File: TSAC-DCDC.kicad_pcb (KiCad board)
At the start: 2 copper layers, 30 parts, among them IC1 PS2811-1-A, Q2 IPB95R450PFD7ATMA1, U1 UCC28C44DR, U3 TL432DBZ

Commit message: Initial PCB layout
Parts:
- moved C2 142.6 mm to (203.1, 70.8)
- moved Rfbt1 141.0 mm to (207.0, 72.3)
- moved Rfbb1 140.7 mm to (207.0, 68.1)
- moved Ropt1 133.2 mm to (198.1, 70.3), turned to -90 degrees
- moved Rtl1 127.1 mm to (198.0, 64.1), turned to 90 degrees
- moved U3 108.2 mm to (198.9, 76.6)
- moved IC1 73.3 mm to (148.5, 77.5)
- moved Rfb4 65.9 mm to (98.3, 96.0)
- moved Rfb3 57.9 mm to (93.9, 86.8)
- moved Rs1 55.7 mm to (98.2, 84.2)
- moved Rs2 55.7 mm to (98.2, 86.8)
- moved Cdd1 54.9 mm to (65.0, 94.2)
- moved Cfb3 48.3 mm to (94.3, 80.5)
- moved Q2 39.3 mm to (119.0, 78.0)
- moved Rdd1 36.7 mm to (80.0, 84.2)
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
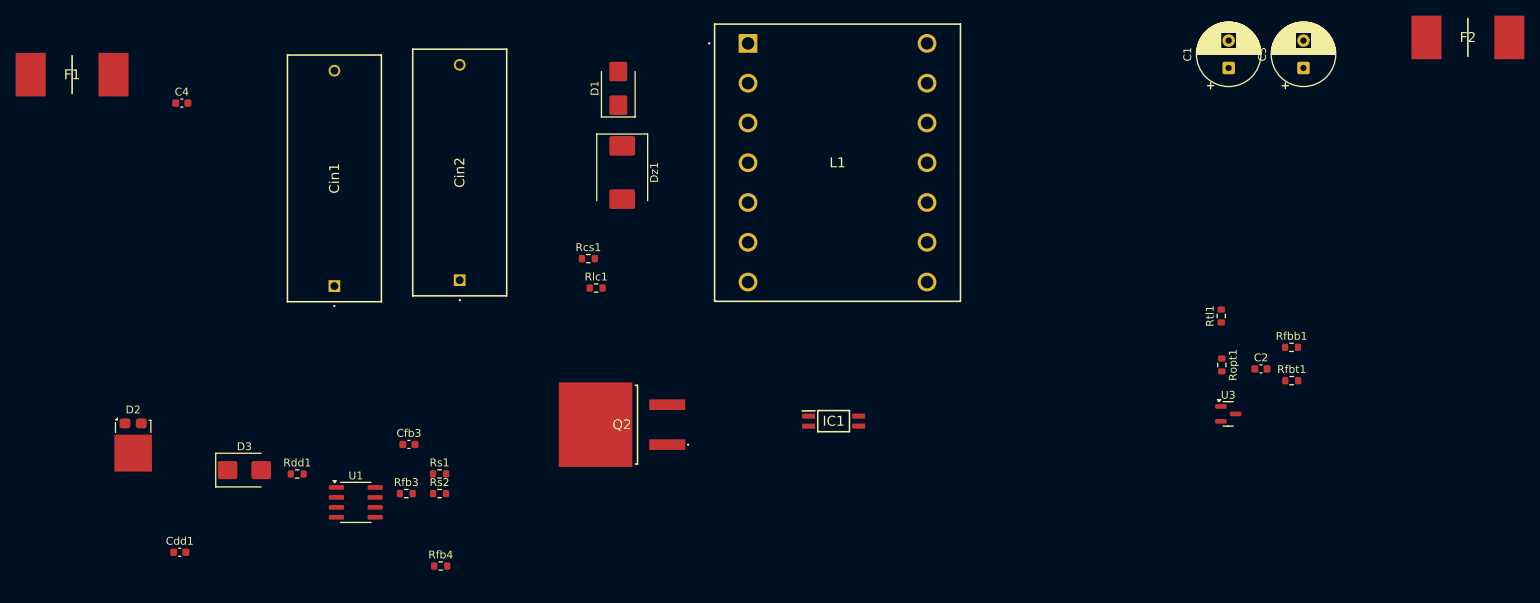
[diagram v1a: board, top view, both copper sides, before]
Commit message: Revert "Initial PCB layout"
This reverts commit eb11546efb0268227655b0bea42a16ad7d7093c5.
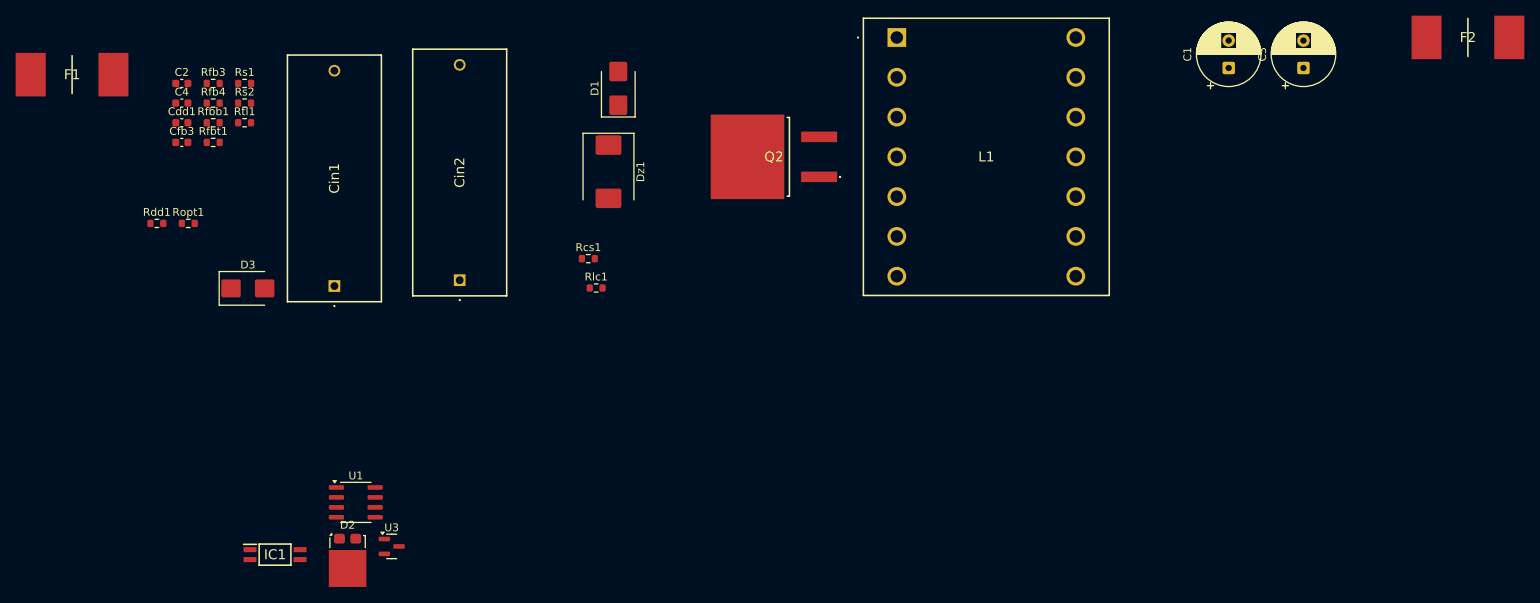
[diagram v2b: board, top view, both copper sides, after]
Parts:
- moved C2 142.6 mm to (65.3, 34.4)
- moved Rfbt1 141.0 mm to (69.3, 41.9)
- moved Rfbb1 140.7 mm to (69.3, 39.4)
- moved Ropt1 133.2 mm to (66.1, 52.2), turned to 0 degrees
- moved Rtl1 127.1 mm to (73.3, 39.4), turned to 0 degrees
- moved U3 108.2 mm to (92.1, 93.5)
- moved IC1 73.3 mm to (77.2, 94.5)
- moved Rfb4 65.9 mm to (69.3, 36.9)
- moved Rfb3 57.9 mm to (69.3, 34.4)
- moved Rs1 55.7 mm to (73.3, 34.4)
- moved Rs2 55.7 mm to (73.3, 36.9)
- moved Cdd1 54.9 mm to (65.3, 39.4)
- moved Cfb3 48.3 mm to (65.3, 41.9)
- moved Q2 39.3 mm to (138.4, 43.8)
- moved Rdd1 36.7 mm to (62.1, 52.2)
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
